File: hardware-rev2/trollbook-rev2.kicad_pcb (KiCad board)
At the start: 2 copper layers, 100 x 100 mm, 8 parts, among them U1 MC68040FC33V, U2 EPF10K50VRC240, U3 39F040, U4 HY57V561620, U5 HY57V561620, U6 AS7C34098, U7 TLC7524, U8 TLC7524

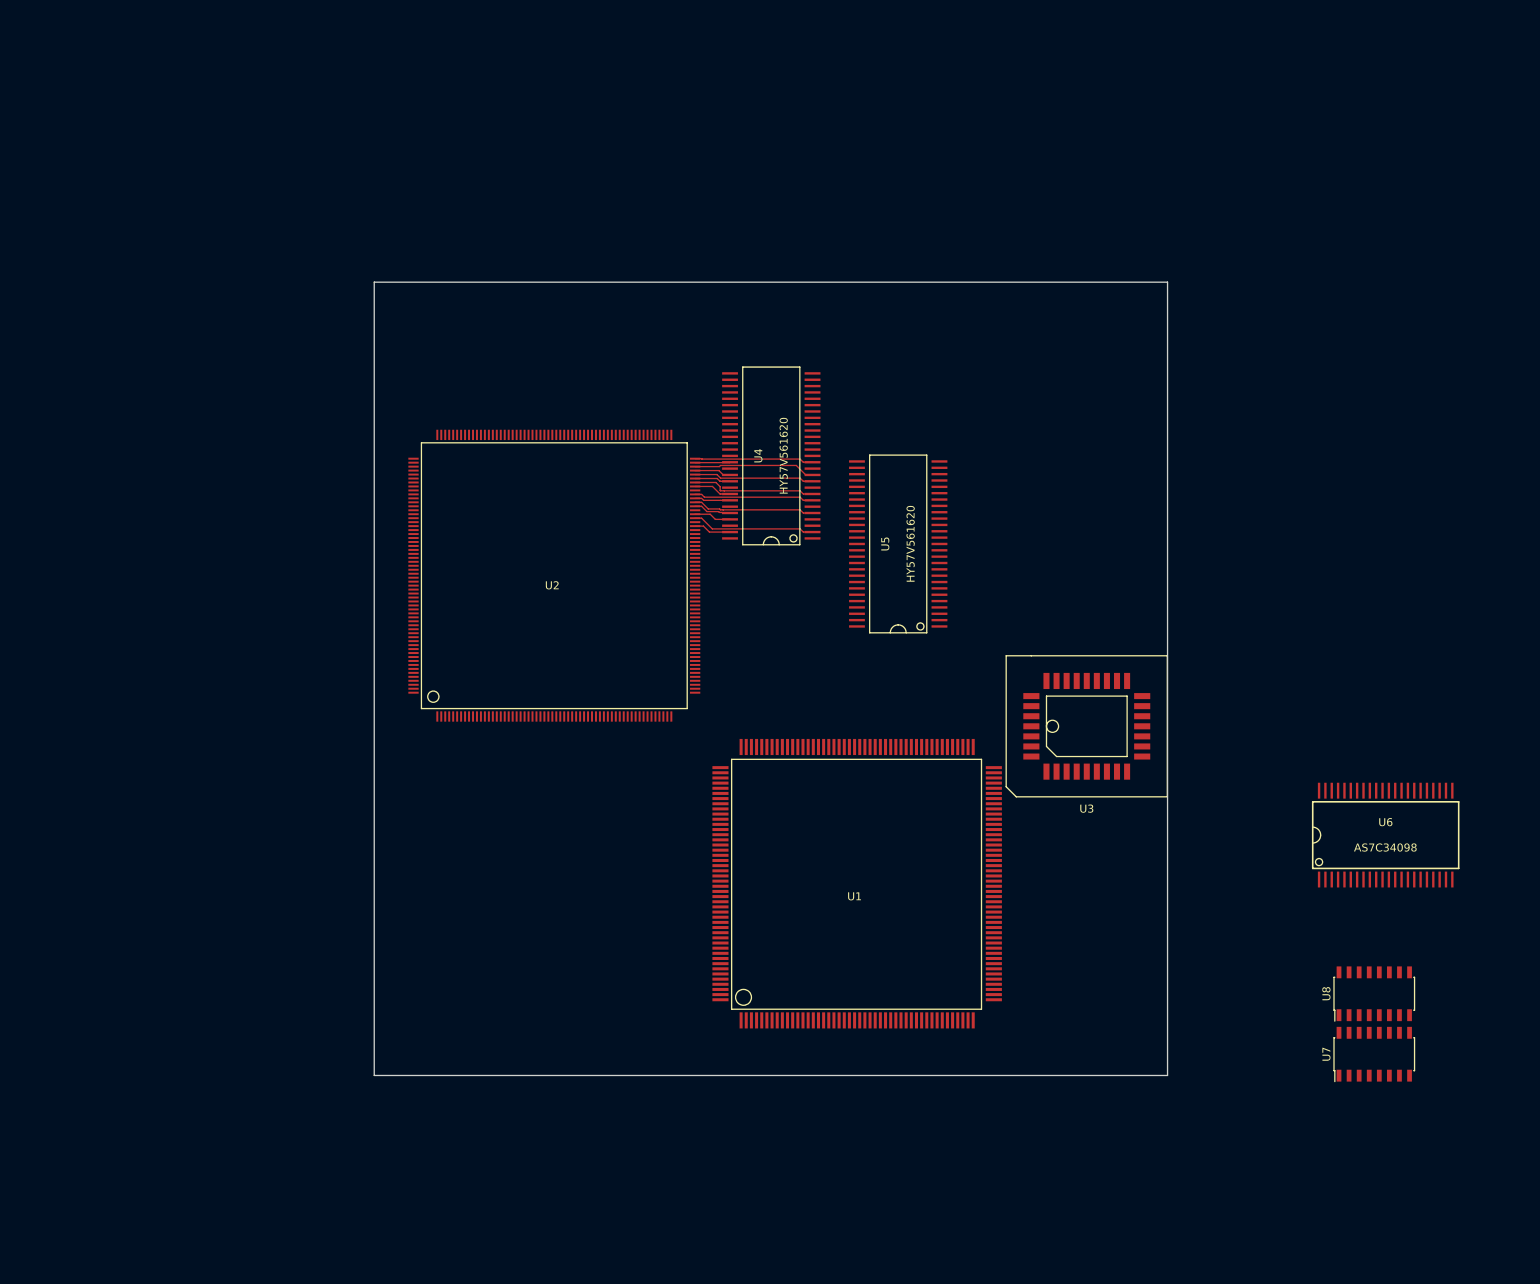
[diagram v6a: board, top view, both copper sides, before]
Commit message: connectec cpu control signals, spi stuff
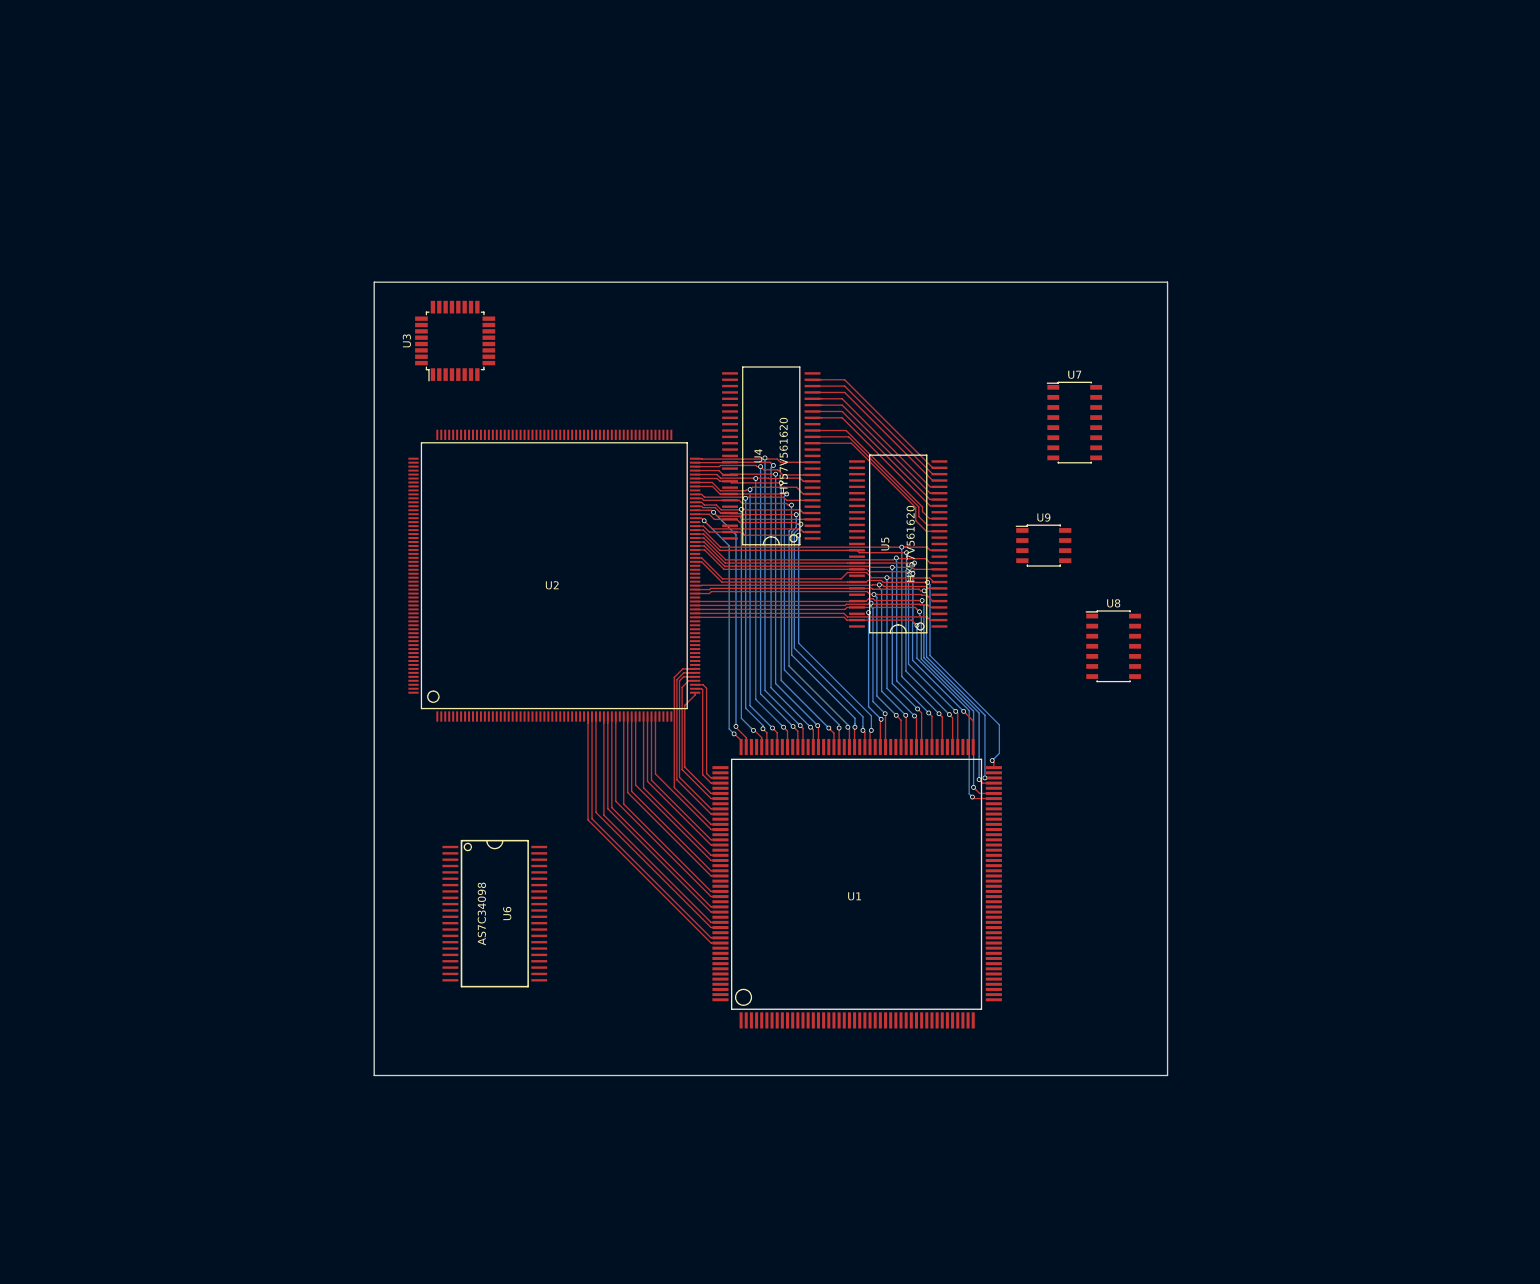
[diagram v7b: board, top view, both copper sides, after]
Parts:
- added U9: S25FL204K0TMFI010, Housings_SOIC:SOIC-8_3.9x4.9mm_Pitch1.27mm, F.Cu at (184.4, 83.2)
- U3: value 39F040 -> EPC2; footprint SMD_Packages:PLCC-32 -> Housings_QFP:TQFP-32_7x7mm_Pitch0.8mm
- U7: value TLC7524 -> 74LVC138
- U8: value TLC7524 -> MCP4902; footprint Housings_SOIC:SOIC-16_3.9x9.9mm_Pitch1.27mm -> Housings_SOIC:SOIC-14_3.9x8.7mm_Pitch1.27mm
- moved U6 112.7 mm to (115.2, 129.6), turned to 270 degrees
- moved U3 93.3 mm to (110.2, 57.4)
- moved U7 88.1 mm to (188.3, 67.7), turned to 0 degrees
- moved U8 54.8 mm to (193.2, 95.9), turned to 0 degrees
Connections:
- U2 pad 12: (no net) -> /LLA5
- U2 pad 121: (no net) -> /CONF_INIT
- U2 pad 123: (no net) -> GND
- U2 pad 124: (no net) -> GND
- U2 pad 126: (no net) -> /RAMCKE
- U2 pad 127: (no net) -> /RAMCLK
- U2 pad 128: (no net) -> /RAM0UDQM
- U2 pad 129: (no net) -> /RAM0LDQM
- U2 pad 13: (no net) -> /LLA6
- U2 pad 131: (no net) -> /RAMWE
- U2 pad 132: (no net) -> /RAM0CS
- U2 pad 133: (no net) -> /RAMRAS
- U2 pad 134: (no net) -> /RAMCAS
- U2 pad 136: (no net) -> /RAMB1
- U2 pad 137: (no net) -> /RAMB0
- U2 pad 138: (no net) -> /RAMA12
- U2 pad 139: (no net) -> /RAMA11
- U2 pad 14: (no net) -> /LLA7
- U2 pad 141: (no net) -> /RAMA10
- U2 pad 142: (no net) -> /RAMA9
- U2 pad 143: (no net) -> /RAMA8
- U2 pad 144: (no net) -> /RAMA7
- U2 pad 146: (no net) -> /RAMA6
- U2 pad 147: (no net) -> /RAMA5
- U2 pad 148: (no net) -> /RAMA4
- U2 pad 149: (no net) -> /RAMA3
- U2 pad 15: (no net) -> /LLA8
- U2 pad 151: (no net) -> /RAMA2
- U2 pad 152: (no net) -> /RAMA1
- U2 pad 153: (no net) -> /RAMA0
- U2 pad 154: (no net) -> /RAM1UDQM
- U2 pad 156: (no net) -> /RAM1LDQM
- U2 pad 157: (no net) -> /RAM1CS
- U2 pad 17: (no net) -> /LLA9
- U2 pad 178: (no net) -> GND
- U2 pad 179: (no net) -> /CONF_CLK
- U2 pad 18: (no net) -> /LLA10
- U2 pad 180: (no net) -> /CONF_DATA
- U2 pad 19: (no net) -> /LLA11
- U2 pad 2: (no net) -> /CONF_CS
- U2 pad 20: (no net) -> /LLA12
- U2 pad 21: (no net) -> /LLA13
- U2 pad 219: (no net) -> /LLD15
- U2 pad 220: (no net) -> /LLD14
- U2 pad 221: (no net) -> /LLD13
- U2 pad 222: (no net) -> /LLD12
- U2 pad 223: (no net) -> /LLD11
- U2 pad 225: (no net) -> /LLD10
- U2 pad 226: (no net) -> /LLD9
- U2 pad 227: (no net) -> /LLD8
- U2 pad 228: (no net) -> /LLD7
- U2 pad 229: (no net) -> /LLD6
- U2 pad 230: (no net) -> /LLD5
- U2 pad 231: (no net) -> /LLD4
- U2 pad 233: (no net) -> /LLD3
- U2 pad 234: (no net) -> /LLD2
- U2 pad 235: (no net) -> /LLD1
- U2 pad 237: (no net) -> /LLD0
- U2 pad 24: (no net) -> /LLA14
- U2 pad 25: (no net) -> /LLA15
- U2 pad 28: (no net) -> /LLA16
- U2 pad 29: (no net) -> /LLA17
- U2 pad 30: (no net) -> /LLA18
- U2 pad 31: (no net) -> /LLCE
- U2 pad 33: (no net) -> /LLWE
- U2 pad 34: (no net) -> /LLLB
- U2 pad 35: (no net) -> /LLUB
- U2 pad 36: (no net) -> /LLOE
- U2 pad 6: (no net) -> /LLA1
- U2 pad 60: (no net) -> /CONF_OE
- U2 pad 7: (no net) -> /LLA2
- U2 pad 8: (no net) -> /LLA3
- U2 pad 80: /D16 -> /D31
- U2 pad 81: /D31 -> /D16
- U2 pad 9: (no net) -> /LLA4
- U3 pad 1: /A18 -> (no net)
- U3 pad 10: /A2 -> /CONF_CS
- U3 pad 13: /ROMD0 -> (no net)
- U3 pad 14: /ROMD1 -> (no net)
- U3 pad 15: /ROMD2 -> (no net)
- U3 pad 16: GND -> /CONF_INIT
- U3 pad 17: /ROMD3 -> +3V3
- U3 pad 18: /ROMD4 -> (no net)
- U3 pad 19: /ROMD5 -> (no net)
- U3 pad 2: /A16 -> /CONF_CLK
- U3 pad 20: /ROMD6 -> (no net)
- U3 pad 21: /ROMD7 -> (no net)
- U3 pad 23: /A10 -> +3V3
- U3 pad 25: /A11 -> (no net)
- U3 pad 26: /A9 -> (no net)
- U3 pad 27: /A8 -> +3V3
- U3 pad 28: /A13 -> (no net)
- U3 pad 29: /A14 -> (no net)
- U3 pad 3: /A15 -> +3V3
- U3 pad 30: /A17 -> (no net)
- U3 pad 31: (no net) -> /CONF_DATA
- U3 pad 32: +3V3 -> (no net)
- U3 pad 4: /A12 -> (no net)
- U3 pad 5: /A7 -> (no net)
- U3 pad 6: /A6 -> (no net)
- U3 pad 7: /A5 -> /CONF_OE
- U3 pad 8: /A4 -> (no net)
- U3 pad 9: /A3 -> (no net)
- U4 pad 15: (no net) -> /RAM0LDQM
- U4 pad 19: (no net) -> /RAM0CS
- U4 pad 39: (no net) -> /RAM0UDQM
- U5 pad 15: (no net) -> /RAM1LDQM
- U5 pad 19: (no net) -> /RAM1CS
- U5 pad 39: (no net) -> /RAM1UDQM
- U6 pad 1: (no net) -> /LLA1
- U6 pad 10: (no net) -> /LLD3
- U6 pad 13: (no net) -> /LLD4
- U6 pad 14: (no net) -> /LLD5
- U6 pad 15: (no net) -> /LLD6
- U6 pad 16: (no net) -> /LLD7
- U6 pad 17: (no net) -> /LLWE
- U6 pad 18: (no net) -> /LLA6
- U6 pad 19: (no net) -> /LLA7
- U6 pad 2: (no net) -> /LLA2
- U6 pad 20: (no net) -> /LLA8
- U6 pad 21: (no net) -> /LLA9
- U6 pad 22: (no net) -> /LLA10
- U6 pad 23: (no net) -> /LLA11
- U6 pad 24: (no net) -> /LLA12
- U6 pad 25: (no net) -> /LLA13
- U6 pad 26: (no net) -> /LLA14
- U6 pad 27: (no net) -> /LLA15
- U6 pad 3: (no net) -> /LLA3
- U6 pad 39: (no net) -> /LLLB
- U6 pad 4: (no net) -> /LLA4
- U6 pad 40: (no net) -> /LLUB
- U6 pad 41: (no net) -> /LLOE
- U6 pad 42: (no net) -> /LLA16
- U6 pad 43: (no net) -> /LLA17
- U6 pad 44: (no net) -> /LLA18
- U6 pad 5: (no net) -> /LLA5
- U6 pad 6: (no net) -> /LLCE
- U6 pad 7: (no net) -> /LLD0
- U6 pad 8: (no net) -> /LLD1
- U6 pad 9: (no net) -> /LLD2
- U7 pad 10: /ROMD1 -> (no net)
- U7 pad 11: /ROMD0 -> (no net)
- U7 pad 13: /DACWR -> (no net)
- U7 pad 4: /ROMD7 -> (no net)
- U7 pad 5: /ROMD6 -> (no net)
- U7 pad 6: /ROMD5 -> (no net)
- U7 pad 7: /ROMD4 -> (no net)
- U7 pad 8: /ROMD3 -> GND
- U7 pad 9: /ROMD2 -> (no net)
- U8 pad 10: /ROMD1 -> (no net)
- U8 pad 11: /ROMD0 -> (no net)
- U8 pad 13: /DACWR -> (no net)
- U8 pad 4: /ROMD7 -> (no net)
- U8 pad 5: /ROMD6 -> (no net)
- U8 pad 6: /ROMD5 -> (no net)
- U8 pad 7: /ROMD4 -> (no net)
- U8 pad 8: /ROMD3 -> (no net)
- U8 pad 9: /ROMD2 -> (no net)
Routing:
- net /D23: track 0.00 -> 59.8 mm, vias 0 -> 2
- net /D27: track 0.00 -> 58.1 mm, vias 0 -> 2
- net /D22: track 0.00 -> 57.9 mm, vias 0 -> 2
- net /D28: track 0.00 -> 56.9 mm, vias 0 -> 2
- net /D31: track 0.00 -> 56.5 mm, vias 0 -> 2
- net /D30: track 0.00 -> 56.5 mm, vias 0 -> 2
- net /D29: track 0.00 -> 56.4 mm, vias 0 -> 2
- net /D21: track 0.00 -> 56.2 mm, vias 0 -> 2
- net /D25: track 0.00 -> 54.8 mm, vias 0 -> 2
- net /D20: track 0.85 -> 55.6 mm, vias 0 -> 2
- net /D24: track 0.00 -> 54.6 mm, vias 0 -> 2
- net /D26: track 0.00 -> 53.7 mm, vias 0 -> 2
- net /D19: track 0.00 -> 52.9 mm, vias 0 -> 2
- net /D18: track 0.00 -> 52.0 mm, vias 0 -> 2
- net /D17: track 0.00 -> 49.9 mm, vias 0 -> 2
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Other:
- copper layers 2 -> 4
